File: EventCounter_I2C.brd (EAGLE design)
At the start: 38.7 x 20.8 mm, 37 parts, among them J1 CONN_42.54_SCREW, J2 CONN_32.54_SCREW, Q1 DMG3404, Q2 FDN360P, Q3 2N7002, U10 TXS0102DQM, U11 TPS7A0533DBV, U4 TLV3691DCK, U7 SN74AUP1G34SC70, U8 SN74AUP3G34DCU, U9 ATTINY441/841VQFN

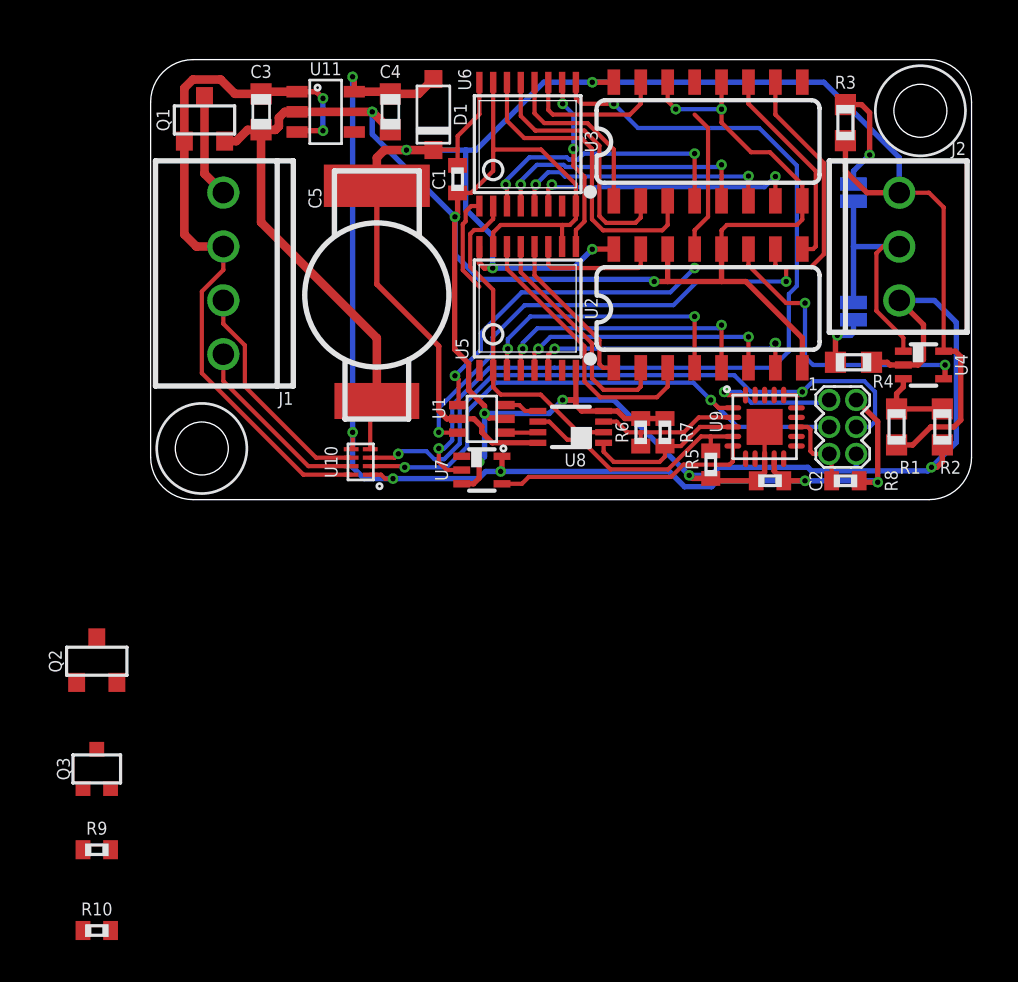
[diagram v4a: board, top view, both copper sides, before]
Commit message: Routing and design update for v1.1
Cleanup/verification required before sending to fab
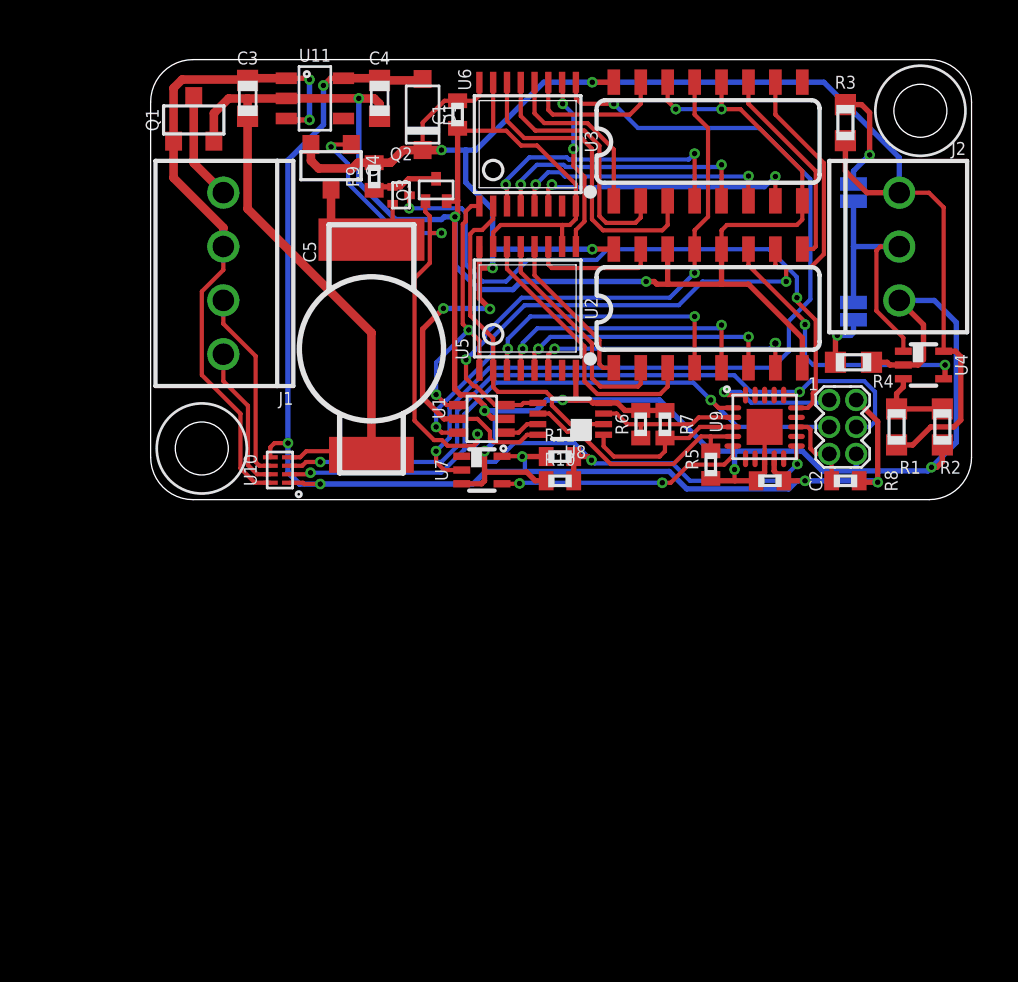
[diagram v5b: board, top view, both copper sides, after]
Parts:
- added Q4: MOSFET_PCH-NX2301P, bschulz:SOT23-3
- added R11: 10k, bschulz_passives:R0402
- Q2: value FDN360P -> MOSFET_PCH-RZM001P02; device bschulz:SOT23-3 -> bschulz:SOT723
- Q3: value 2N7002 -> MOSFET-NCH-RE1C002UN; device bschulz:SOT323 -> bschulz:SC-89
- R10, R9: value (none) -> 1M
- moved R9 34.3 mm to (10.5, 15.2), turned to 90 degrees
- moved Q3 31.6 mm to (13.5, 14.6)
- moved R10 30.4 mm to (19.3, 0.89)
- moved Q2 26.2 mm to (11.8, 14.4), turned to 270 degrees
- moved U10 3.83 mm to (6.10, 1.40)
- moved C1 3.05 mm to (14.5, 18.2)
- moved C5 2.55 mm to (10.4, 7.11)
- moved C3 0.90 mm to (4.57, 18.9)
- moved C4 0.81 mm to (10.8, 18.9)
- moved U11 0.81 mm to (7.75, 18.9)
- moved D1 0.51 mm to (12.8, 18.2)
- moved Q1 0.51 mm to (2.03, 17.9)
- moved R6 0.38 mm to (23.1, 3.56)
- moved R7 0.38 mm to (24.3, 3.56)
- moved U8 0.38 mm to (19.8, 3.81)
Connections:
- new net CHARGE_SW: Q3.1, Q4.1, R10.2, R11.2, U9.11
- new net V_SYS: C1.1, D1.CAT, J2.1, Q4.2, R1.2, R3.2, R9.2, U1.5, U2.16, U3.16, U4.5, U5.16, U6.16, U8.8
- net 3V3: now also R11.1
- net VIN+: no longer Q3.1, R10.2
- net V_CAP: now also Q4.3; no longer C1.1, D1.CAT, J2.1, R1.2, R3.2, R9.2, U1.5, U2.16, U3.16, U4.5, U5.16, U6.16, U8.8
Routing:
- net V_SYS: track 0.00 -> 89.6 mm, vias 0 -> 6
- net V_CAP: track 90.3 -> 7.72 mm, vias 4 -> 0
- net CHARGE_SW: track 0.00 -> 44.4 mm, vias 0 -> 5
- net V_CAP_READ: track 0.00 -> 30.2 mm, vias 0 -> 2
- net LOAD: track 8.53 -> 27.0 mm, vias 0 -> 2
- net GND: track 163.2 -> 179.3 mm
- net 3V3: track 58.9 -> 65.8 mm
- net !LOAD: track 20.0 -> 13.6 mm
- net SCL: track 26.4 -> 30.3 mm
- net SDA: track 30.8 -> 34.3 mm
- net N$21: track 0.00 -> 3.19 mm
- net VIN+: track 34.3 -> 31.5 mm
- net SCL_HV: track 8.96 -> 6.94 mm
- net SDA_HV: track 10.9 -> 9.02 mm
- net DATA: track 42.7 -> 43.2 mm
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
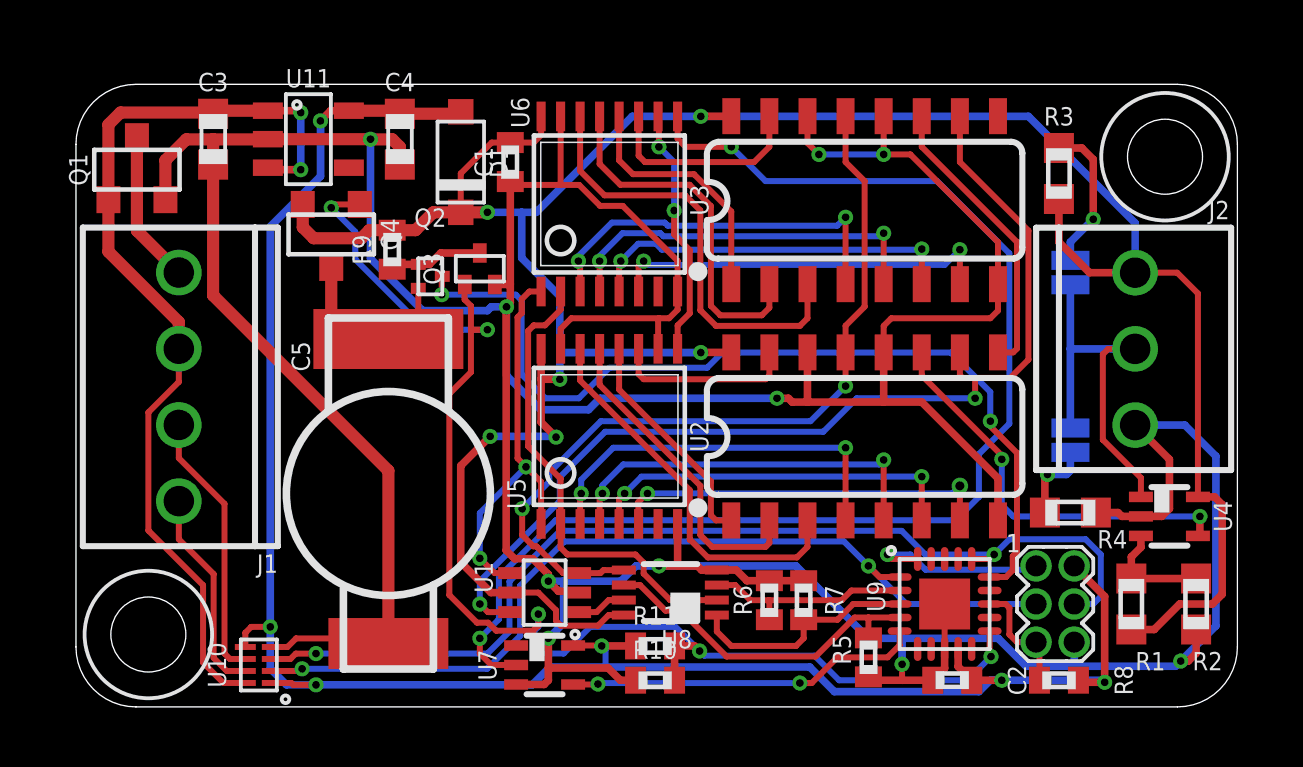
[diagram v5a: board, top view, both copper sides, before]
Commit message: Minor cleanup, generated gerbers, sent v1.1 to fab
Minor cleanup and rearranging silkscreen names, changed jumper configuration
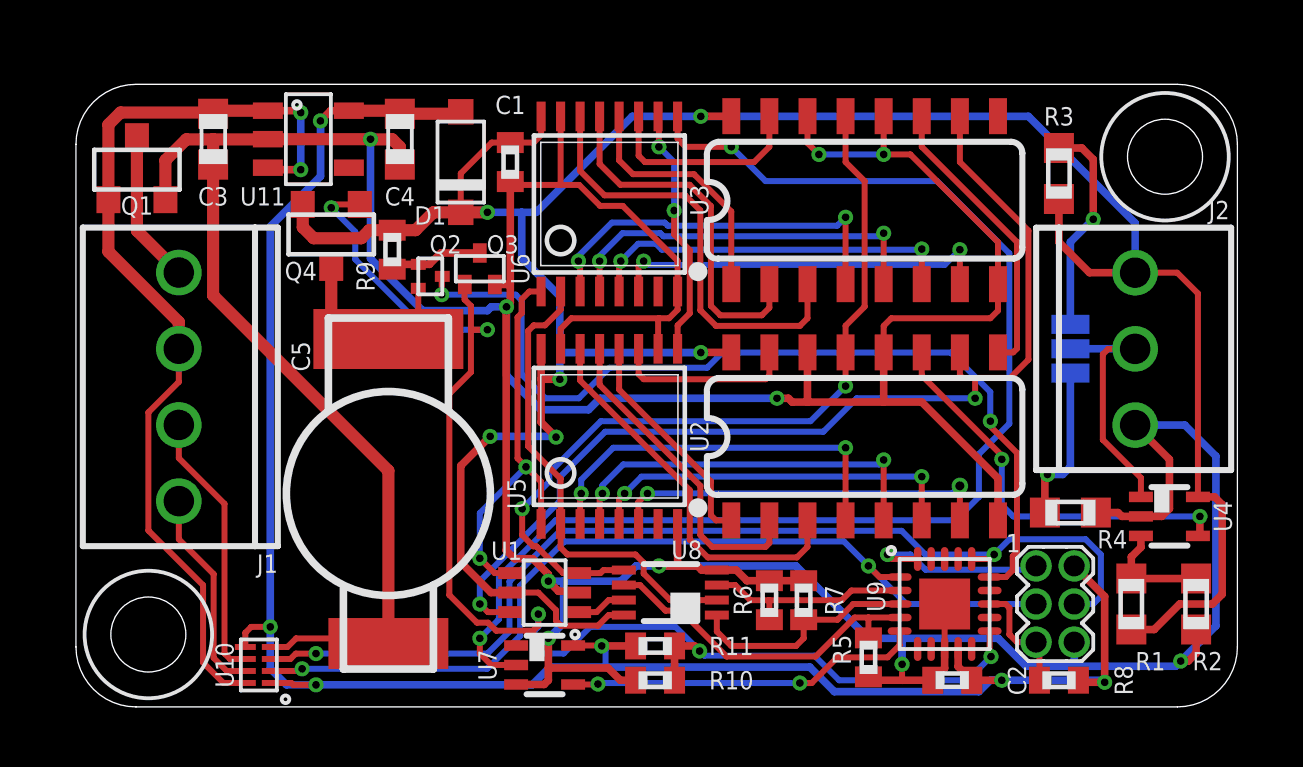
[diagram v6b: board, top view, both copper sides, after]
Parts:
- removed JP1, JP2: JUMPER-SMT_2_NC_PASTE_SILK, SparkFun-Jumpers:SMT-JUMPER_2_NC_PASTE_SILK
- added JP0: JUMPER-SMT_3_1-NC_PASTE_SILK, SparkFun-Jumpers:SMT-JUMPER_3_1-NC_PASTE_SILK
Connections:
- net N$19: now also JP0.3; no longer JP2.2
- net N$20: now also JP0.1; no longer JP1.2
- net PULSE: now also JP0.2; no longer JP1.1, JP2.1
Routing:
- net PULSE: track 13.4 -> 8.60 mm
- net N$19: track 2.73 -> 5.30 mm
- net N$20: track 4.98 -> 7.11 mm
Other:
- board text removed: "J1"

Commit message: Minor value updates
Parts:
- R8: value (none) -> 10k
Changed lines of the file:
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@@
 <layer number="27" name="tValues" color="7" fill="1" visible="no" active="yes"/>
 <layer number="28" name="bValues" color="7" fill="1" visible="no" active="yes"/>
-<layer number="29" name="tStop" color="7" fill="3" visible="yes" active="yes"/>
+<layer number="29" name="tStop" color="7" fill="3" visible="no" active="yes"/>
 <layer number="30" name="bStop" color="7" fill="6" visible="no" active="yes"/>
 <layer number="31" name="tCream" color="7" fill="4" visible="no" active="yes"/>
@@
 <layer number="37" name="tTest" color="7" fill="1" visible="no" active="yes"/>
 <layer number="38" name="bTest" color="7" fill="1" visible="no" active="yes"/>
-<layer number="39" name="tKeepout" color="4" fill="11" visible="yes" active="yes"/>
+<layer number="39" name="tKeepout" color="4" fill="11" visible="no" active="yes"/>
 <layer number="40" name="bKeepout" color="1" fill="11" visible="yes" active="yes"/>
-<layer number="41" name="tRestrict" color="4" fill="10" visible="yes" active="yes"/>
+<layer number="41" name="tRestrict" color="4" fill="10" visible="no" active="yes"/>
 <layer number="42" name="bRestrict" color="1" fill="10" visible="yes" active="yes"/>
 <layer number="43" name="vRestrict" color="2" fill="10" visible="no" active="yes"/>
@@
 <attribute name="VALUE" x="15.621" y="5.461" size="0.6096" layer="27" font="vector" ratio="15" rot="R180" align="center"/>
 </element>
-<element name="R8" library="bschulz_passives" package="R0402" value="" x="32.766" y="0.889" smashed="yes">
+<element name="R8" library="bschulz_passives" package="R0402" value="10k" x="32.766" y="0.889" smashed="yes">
 <attribute name="DIGIKEY" value="311-10KJRCT-ND" x="32.766" y="0.889" size="1.778" layer="27" display="off"/>
 <attribute name="MF" value="Yageo" x="32.766" y="0.889" size="1.778" layer="27" display="off"/>

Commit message: Updated part values
Switched values of `R10` and `R11`, values were erroneously switched which resulted in the capacitor being connected to the ADC input during sleep/off state, causing significant power draw
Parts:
- R10: value 1M -> 10k
- R11: value 10k -> 1M
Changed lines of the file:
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@@
 <attribute name="VALUE_PART" value="1M" x="10.541" y="15.24" size="1.778" layer="27" rot="R90" display="off"/>
 </element>
-<element name="R10" library="bschulz_passives" package="R0402" value="1M" x="19.304" y="0.889" smashed="yes">
-<attribute name="DIGIKEY" value="311-1.00MLRCT-ND" x="19.304" y="0.889" size="1.778" layer="27" display="off"/>
+<element name="R10" library="bschulz_passives" package="R0402" value="10k" x="19.304" y="0.889" smashed="yes">
+<attribute name="DIGIKEY" value="311-10KJRCT-ND" x="19.304" y="0.889" size="1.778" layer="27" display="off"/>
 <attribute name="MF" value="Yageo" x="19.304" y="0.889" size="1.778" layer="27" display="off"/>
-<attribute name="MPN" value="RC0402FR-071ML" x="19.304" y="0.889" size="1.778" layer="27" display="off"/>
+<attribute name="MPN" value="RC0402JR-0710KL" x="19.304" y="0.889" size="1.778" layer="27" display="off"/>
 <attribute name="NAME" x="21.844" y="0.889" size="0.6096" layer="25" font="vector" ratio="15" align="center"/>
 <attribute name="VALUE" x="19.304" y="-0.127" size="0.6096" layer="27" font="vector" ratio="15" align="center"/>
-<attribute name="VALUE_PART" value="1M" x="19.304" y="0.889" size="1.778" layer="27" display="off"/>
+<attribute name="VALUE_PART" value="10k" x="19.304" y="0.889" size="1.778" layer="27" display="off"/>
 </element>
 <element name="Q4" library="bschulz" package="SOT23-3" value="MOSFET_PCH-NX2301P" x="8.509" y="15.748" smashed="yes" rot="R180">
@@
 <attribute name="VALUE" x="6.858" y="15.748" size="0.6096" layer="27" font="vector" ratio="20" rot="R270" align="top-center"/>
 </element>
-<element name="R11" library="bschulz_passives" package="R0402" value="10k" x="19.304" y="2.032" smashed="yes">
-<attribute name="DIGIKEY" value="311-10KJRCT-ND" x="19.304" y="2.032" size="0.6096" layer="27" font="vector" ratio="15" display="off"/>
+<element name="R11" library="bschulz_passives" package="R0402" value="1M" x="19.304" y="2.032" smashed="yes">
+<attribute name="DIGIKEY" value="311-1.00MLRCT-ND" x="19.304" y="2.032" size="0.6096" layer="27" font="vector" ratio="15" display="off"/>
 <attribute name="MF" value="Yageo" x="19.304" y="2.032" size="0.6096" layer="27" font="vector" ratio="15" display="off"/>
-<attribute name="MPN" value="RC0402JR-0710KL" x="19.304" y="2.032" size="0.6096" layer="27" font="vector" ratio="15" display="off"/>
+<attribute name="MPN" value="RC0402FR-071ML" x="19.304" y="2.032" size="0.6096" layer="27" font="vector" ratio="15" display="off"/>
 <attribute name="NAME" x="21.844" y="2.032" size="0.6096" layer="25" font="vector" ratio="15" align="center"/>
 <attribute name="VALUE" x="19.304" y="1.016" size="0.6096" layer="27" font="vector" ratio="15" align="center"/>
-<attribute name="VALUE_PART" value="10k" x="19.304" y="2.032" size="0.6096" layer="27" font="vector" ratio="15" display="off"/>
+<attribute name="VALUE_PART" value="1M" x="19.304" y="2.032" size="0.6096" layer="27" font="vector" ratio="15" display="off"/>
 </element>
 <element name="JP0" library="SparkFun-Jumpers" library_urn="urn:adsk.eagle:library:528" package="SMT-JUMPER_3_1-NC_PASTE_SILK" package3d_urn="urn:adsk.eagle:package:39293/1" value="JUMPER-SMT_3_1-NC_PASTE_SILK" x="33.147" y="11.938" smashed="yes" rot="MR270">
